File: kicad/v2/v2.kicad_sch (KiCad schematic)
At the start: 110 parts, among them U1 Raspberry_Pi_Pico, U2 Raspberry_Pi_Pico

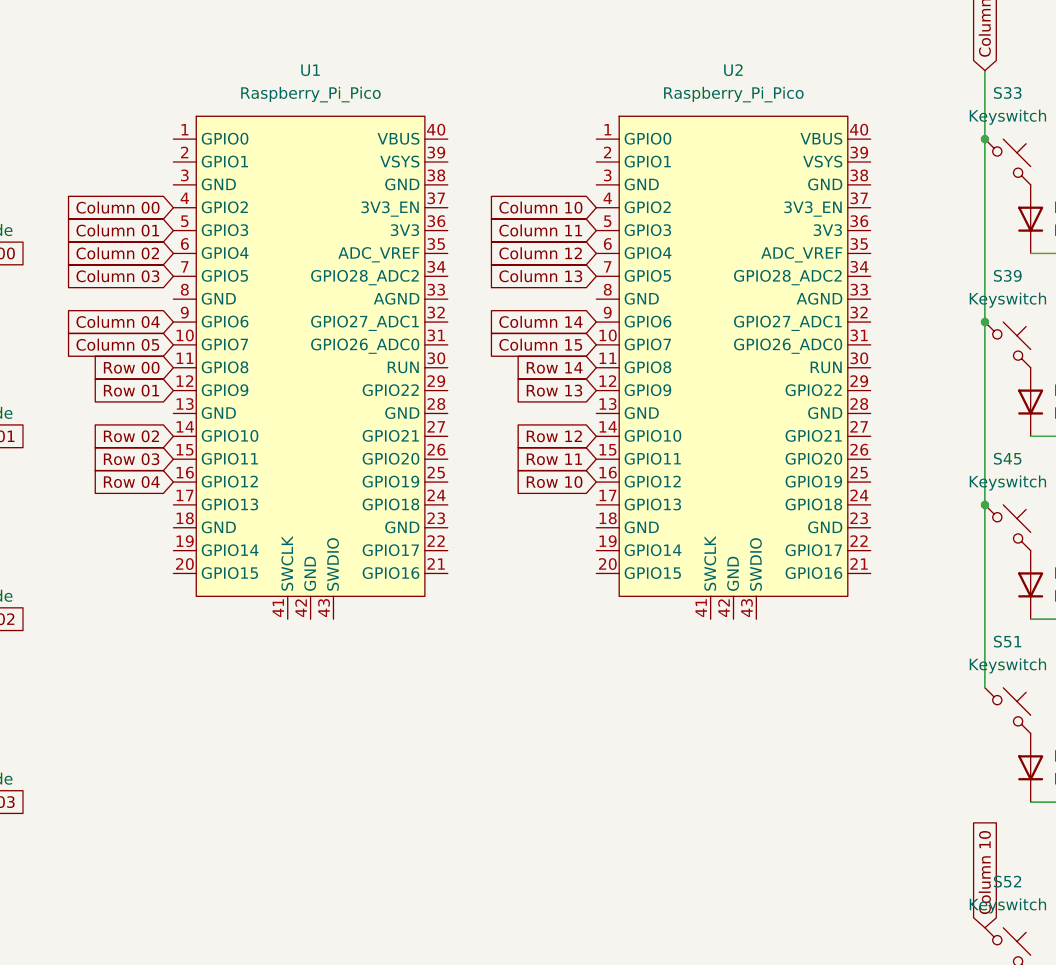
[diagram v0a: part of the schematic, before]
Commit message: add: 3.5mm jacks with very messy wiring
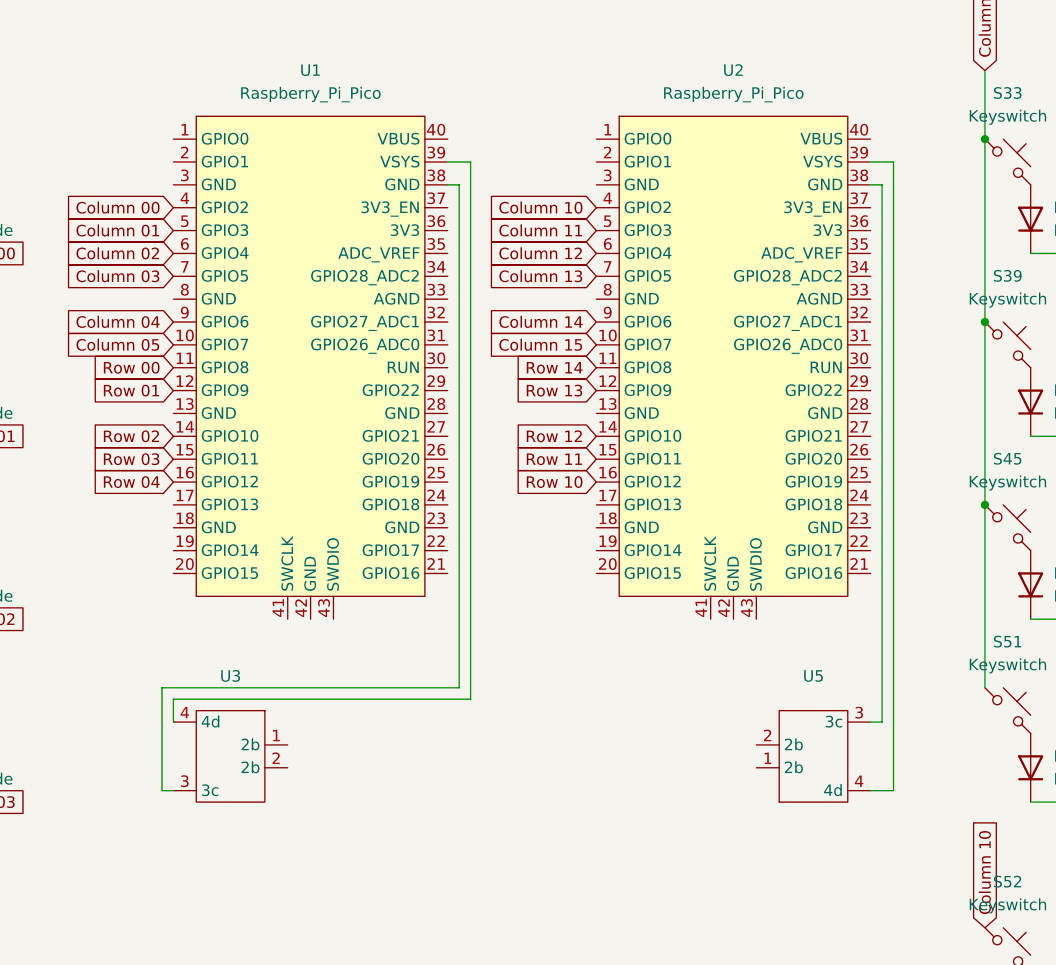
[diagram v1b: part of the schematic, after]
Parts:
- added U3, U5: ~, flosLibrary:Lumberg 1503 29 Klinken-Einbaubuchse, symbol flosLibrary:Lumberg_1503_29_Klinken-Einbaubuchse
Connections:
- net at U2.38 (GND): now also U5.3 (3c)
- net at U2.39 (VSYS): now also U5.4 (4d)
- net at U1.38 (GND): now also U3.3 (3c)
- net at U1.39 (VSYS): now also U3.4 (4d)
